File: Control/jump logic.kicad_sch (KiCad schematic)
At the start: 5 parts

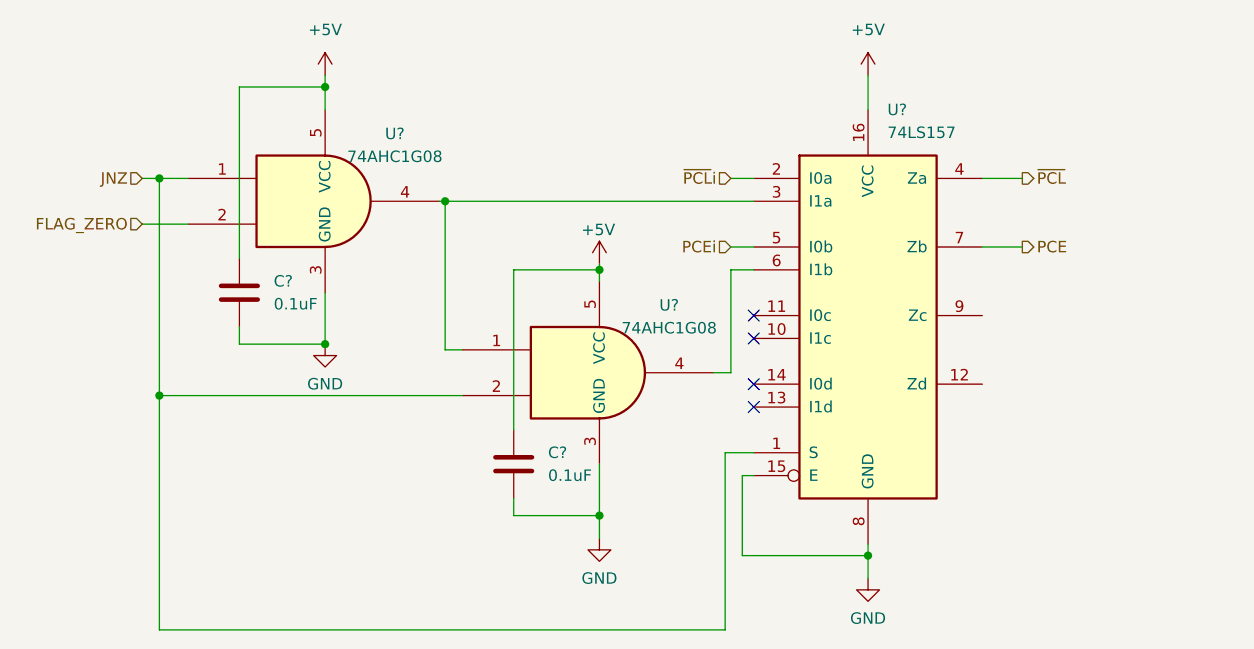
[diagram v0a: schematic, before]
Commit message: Cleanup, added photos and README overhaul
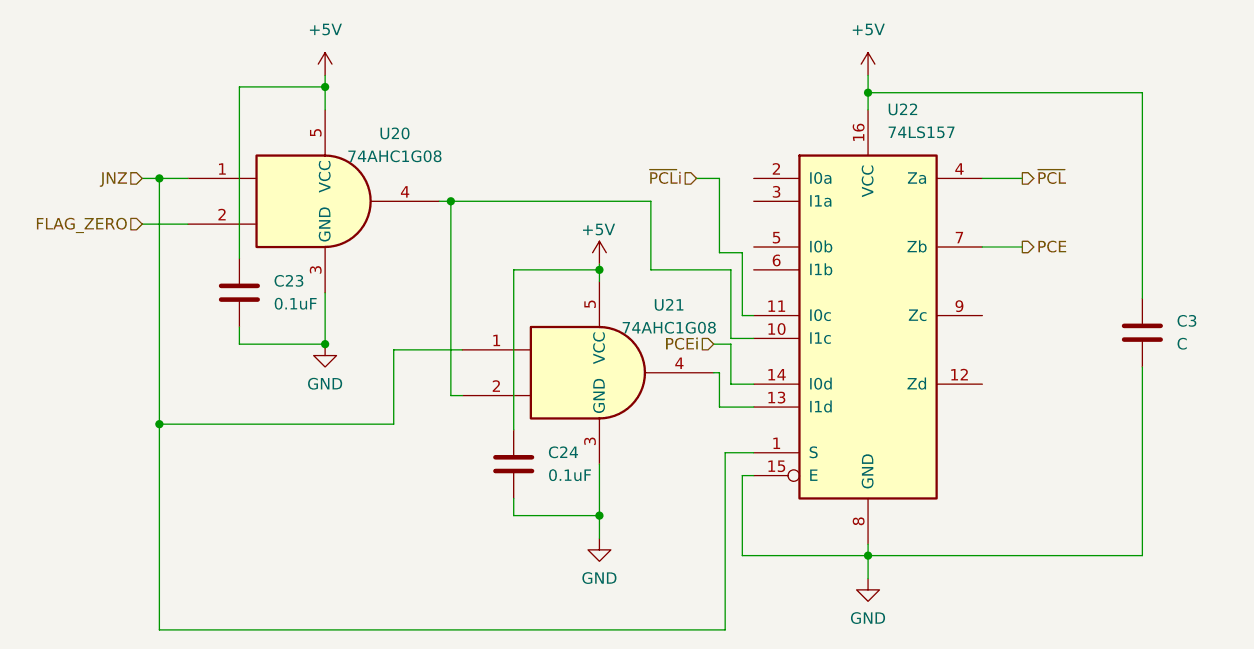
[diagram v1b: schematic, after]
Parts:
- added C3: C, Capacitor_SMD:C_0603_1608Metric, symbol Device:C
- C23, C24: renamed from C?; footprint (none) -> Capacitor_SMD:C_0603_1608Metric
- U20, U21: renamed from U?; footprint (none) -> Package_TO_SOT_SMD:SOT-23-5
- U22: renamed from U?; footprint (none) -> Package_SO:SOIC-16_3.9x9.9mm_P1.27mm
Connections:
- net +5V: now also C3.1
- net GND: now also C3.2
- net JNZ: now also U21.1; no longer U21.2
- net PCEi: now also U22.14 (I0d); no longer U22.5 (I0b)
- net ~{PCL}i: now also U22.11 (I0c); no longer U22.2 (I0a)
- net at U22.10 (I1c): now also U20.4, U21.2
- net at U22.13 (I1d): now also U21.4
- net at U22.6 (I1b): no longer U21.4
- now unconnected: U22.3 (I1a)
- no-connect marks 4 -> 0

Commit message: Finalized Control unit for fabrication
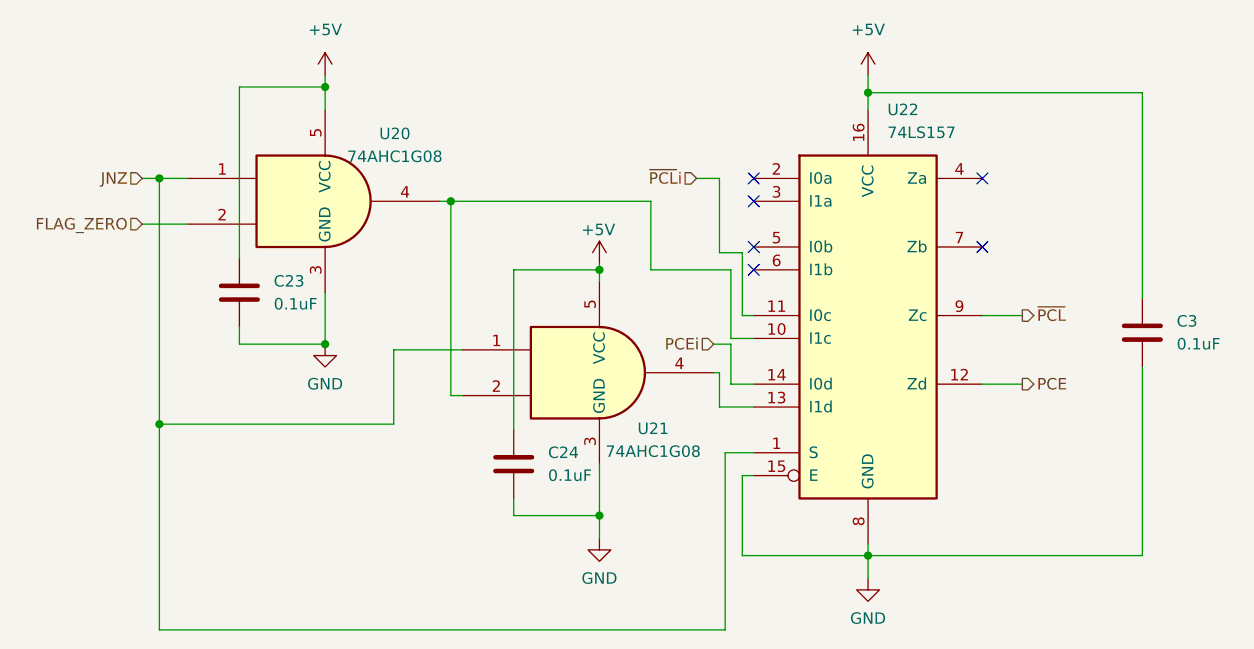
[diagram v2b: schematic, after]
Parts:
- C3: value C -> 0.1uF
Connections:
- net PCE: now also U22.12 (Zd); no longer U22.7 (Zb)
- net ~{PCL}: now also U22.9 (Zc); no longer U22.4 (Za)
- no-connect marks 0 -> 6
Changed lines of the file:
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@@
 		(color 0 0 0 0)
 	)
+	(no_connect
+		(at 119.38 32.385)
+	)
+	(no_connect
+		(at 93.98 42.545)
+	)
+	(no_connect
+		(at 93.98 34.925)
+	)
+	(no_connect
+		(at 93.98 32.385)
+	)
+	(no_connect
+		(at 119.38 40.005)
+	)
+	(no_connect
+		(at 93.98 40.005)
+	)
 	(wire
 		(pts
@@
 	(wire
 		(pts
+			(xy 119.38 47.625) (xy 123.825 47.625)
+		)
+		(stroke
+			(width 0)
+			(type default)
+		)
+	)
+	(wire
+		(pts
 			(xy 53.975 59.69) (xy 53.975 51.435)
 		)
@@
 	(wire
 		(pts
-			(xy 123.825 40.005) (xy 119.38 40.005)
-		)
-		(stroke
-			(width 0)
-			(type default)
-		)
-	)
-	(wire
-		(pts
 			(xy 92.71 40.64) (xy 92.71 47.625)
 		)
@@
 	(wire
 		(pts
+			(xy 123.825 55.245) (xy 119.38 55.245)
+		)
+		(stroke
+			(width 0)
+			(type default)
+		)
+	)
+	(wire
+		(pts
 			(xy 26.035 37.465) (xy 31.115 37.465)
 		)
@@
 		(pts
 			(xy 90.17 53.975) (xy 90.17 57.785)
-		)
-		(stroke
-			(width 0)
-			(type default)
-		)
-	)
-	(wire
-		(pts
-			(xy 119.38 32.385) (xy 123.825 32.385)
 		)
 		(stroke
@@
 		)
 	)
-	(hierarchical_label "PCE"
-		(shape output)
-		(at 123.825 40.005 0)
-		(effects
-			(font
-				(size 1.27 1.27)
-			)
-			(justify left)
-		)
-	)
 	(hierarchical_label "~{PCL}i"
 		(shape input)
@@
 		)
 	)
-	(hierarchical_label "~{PCL}"
-		(shape output)
-		(at 123.825 32.385 0)
-		(effects
-			(font
-				(size 1.27 1.27)
-			)
-			(justify left)
-		)
-	)
 	(hierarchical_label "FLAG_ZERO"
 		(shape input)
@@
 			)
 			(justify right)
+		)
+	)
+	(hierarchical_label "PCE"
+		(shape output)
+		(at 123.825 55.245 0)
+		(effects
+			(font
+				(size 1.27 1.27)
+			)
+			(justify left)
+		)
+	)
+	(hierarchical_label "~{PCL}"
+		(shape output)
+		(at 123.825 47.625 0)
+		(effects
+			(font
+				(size 1.27 1.27)
+			)
+			(justify left)
 		)
 	)
@@
 			)
 		)
-		(property "Value" "C"
+		(property "Value" "0.1uF"
 			(at 140.97 50.7999 0)
 			(effects
@@
 		(dnp no)
 		(property "Reference" "U21"
-			(at 84.582 46.482 0)
+			(at 82.804 60.198 0)
 			(effects
 				(font
@@
 		)
 		(property "Value" "74AHC1G08"
-			(at 84.582 49.022 0)
-			(effects
-				(font
+			(at 82.804 62.738 0)
+			(effects
+				(font
